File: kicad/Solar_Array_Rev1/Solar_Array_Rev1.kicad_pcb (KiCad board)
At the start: 2 copper layers, 46.9 x 29 mm, 24 parts, among them IC2 NUP4202W1_4INPUT_TVS, IC3 NUP4202W1_4INPUT_TVS, P1 PV_IN, P2 CONN_01X07, Q1 Q_NPN_BCE, U1 LTC2990

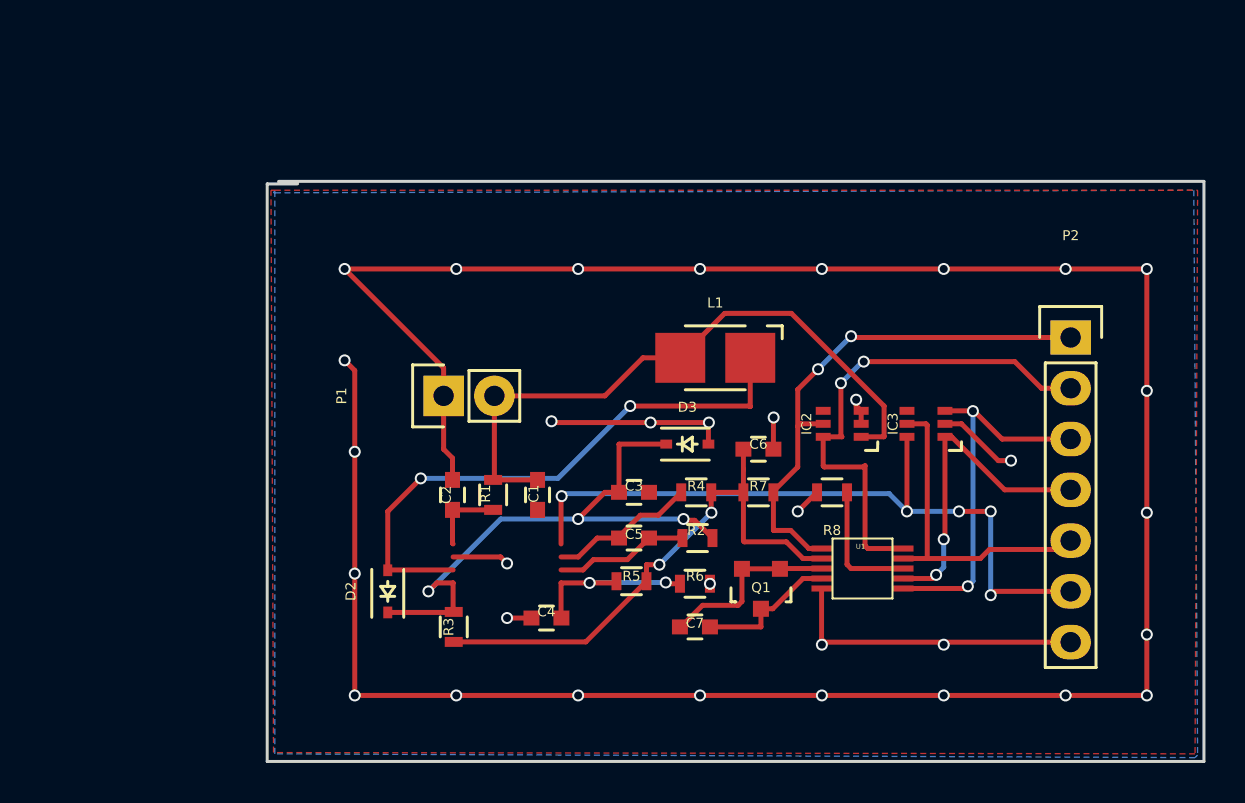
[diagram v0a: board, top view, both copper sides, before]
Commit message: Removed old files, repaired broken schema, finished layout.
-Removed old SVG DRL and  GBR files
-Removed old PDF files
-Fixed broken TVS_4x4 Schematic and updated footprint
-PCB file created
-Board layout finished
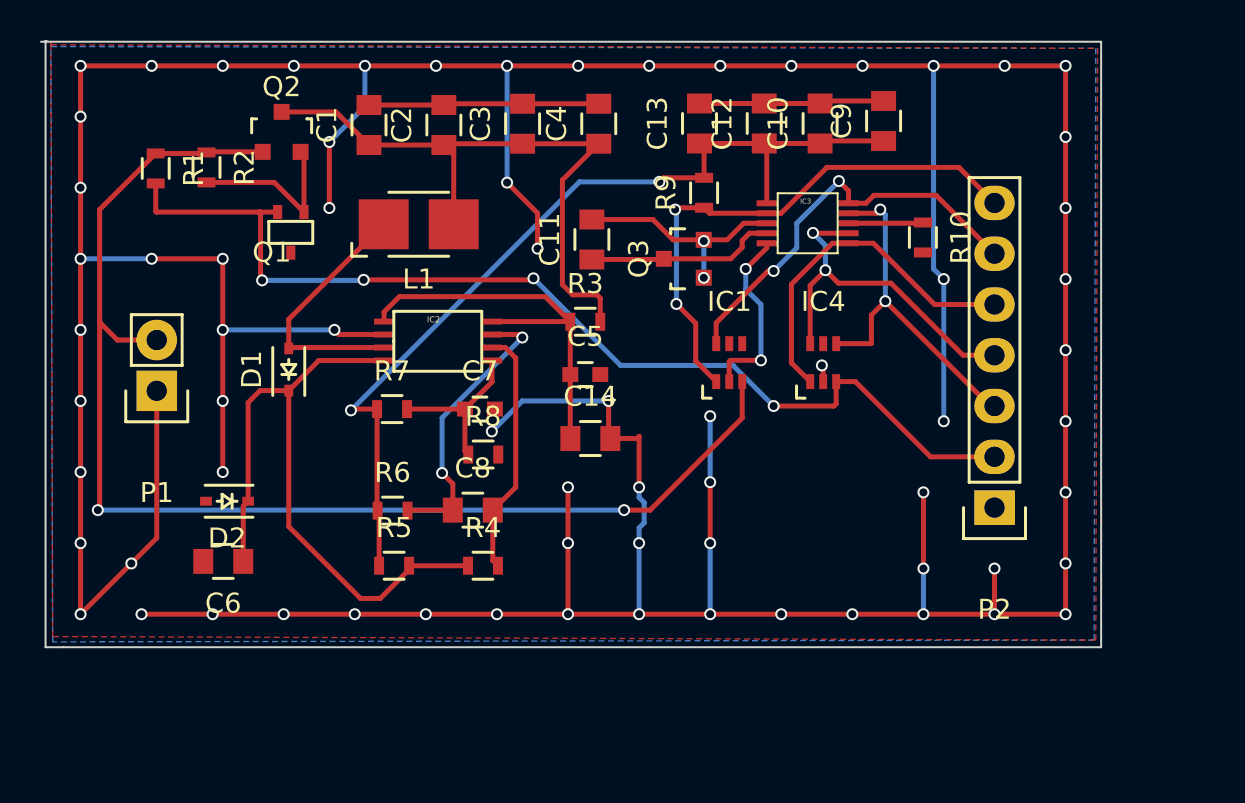
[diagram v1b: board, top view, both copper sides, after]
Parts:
- removed D3: ZENER, Diodes_SMD:SOD-323
- removed U1: LTC2990, Solar:MSOP-10
- added C10: 47u, Capacitors_SMD:C_0805, F.Cu at (151.3, 83.1)
- added C11: 1.2u, Capacitors_SMD:C_0805, F.Cu at (139.9, 89.0)
- added C12: 47u, Capacitors_SMD:C_0805, F.Cu at (148.5, 83.1)
- added C13: 47u, Capacitors_SMD:C_0805, F.Cu at (145.3, 83.1)
- added C14: 1.2u, Capacitors_SMD:C_0805, F.Cu at (139.8, 98.9)
- added C8: 1.2u, Capacitors_SMD:C_0805, F.Cu at (133.9, 102.5)
- added C9: 47u, Capacitors_SMD:C_0805, F.Cu at (154.5, 83.0)
- added D1: D_Schottky, Diodes_SMD:SOD-323, F.Cu at (124.7, 95.5)
- added IC1: TVS_4x4, Solar:SC-70-6, F.Cu at (146.7, 95.1)
- added IC4: TVS_4x4, TO_SOT_Packages_SMD:SC-70-6, F.Cu at (151.4, 95.1)
- added Q2: Q_PMOS_DGS, TO_SOT_Packages_SMD:SOT-23, F.Cu at (124.4, 83.6)
- added Q3: Q_NPN_BCE, TO_SOT_Packages_SMD:SOT-23, F.Cu at (144.5, 89.9)
- added R10: 10k, Resistors_SMD:R_0603, F.Cu at (156.4, 88.8)
- added R9: .3, Resistors_SMD:R_0603, F.Cu at (145.5, 86.6)
- C1, C3: value 216u -> 47u; footprint Capacitors_SMD:C_0603 -> Capacitors_SMD:C_0805
- C2: value 8u -> 47u; footprint Capacitors_SMD:C_0603 -> Capacitors_SMD:C_0805
- C4: value 2u -> 47u; footprint Capacitors_SMD:C_0603 -> Capacitors_SMD:C_0805
- C5: value 1u -> 6.8u
- C6: footprint Capacitors_SMD:C_0603 -> Capacitors_SMD:C_0805
- C7: value 1u -> 2u
- D2: value D_Schottky -> ZENER
- IC2: value NUP4202W1_4INPUT_TVS -> SPV1040; footprint TO_SOT_Packages_SMD:SC-70-6 -> Solar:TSSOP-8
- IC3: value NUP4202W1_4INPUT_TVS -> LTC2990.1; footprint TO_SOT_Packages_SMD:SC-70-6 -> Solar:MSOP-10
- Q1: value Q_NPN_BCE -> Q_NMOS_DGS; footprint TO_SOT_Packages_SMD:SOT-23 -> TO_SOT_Packages_SMD:SC-70
- R1: value 1k -> 10k
- R2: value 1k -> 100k
- R3: value .274 -> 1k
- R5: value 240 -> .274
- R6: value 80 -> 1k
- R7: value .3 -> 240
- R8: value 10k -> 80
- moved R2 30.8 mm to (120.6, 85.3), turned to 270 degrees
- moved Q1 29.5 mm to (124.8, 88.6)
- moved C6 27.4 mm to (121.4, 105.1), turned to 180 degrees
- moved C4 24.9 mm to (140.2, 83.2), turned to 90 degrees
- moved R1 23.5 mm to (118.1, 85.4), turned to 270 degrees
- moved IC2 20.6 mm to (132.2, 94.0), turned to 0 degrees
- moved C1 20.3 mm to (128.7, 83.2), turned to 90 degrees
- moved C3 19.3 mm to (136.4, 83.2), turned to 90 degrees
- moved R7 18.8 mm to (129.9, 97.4), turned to 0 degrees
- moved C2 18.5 mm to (132.5, 83.2)
- moved R8 17.6 mm to (134.4, 99.7), turned to 0 degrees
- moved R3 16.6 mm to (139.5, 93.1), turned to 0 degrees
- moved L1 16.3 mm to (131.2, 88.2), turned to 0 degrees
- moved R6 15.6 mm to (129.9, 102.5)
- moved C7 15.3 mm to (134.3, 97.4), turned to 0 degrees
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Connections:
- C2 pad 1: Net-(C2-Pad1) -> Net-(C1-Pad1)
- C3 pad 1: Net-(C3-Pad1) -> Net-(C1-Pad1)
- C4 pad 1: Net-(C4-Pad1) -> Net-(C1-Pad1)
- C5 pad 1: Net-(C5-Pad1) -> Net-(C14-Pad1)
- C5 pad 2: Net-(C5-Pad2) -> GND
- C7 pad 2: Net-(C7-Pad2) -> GND
- D2 pad 1: Net-(C3-Pad1) -> Net-(C6-Pad1)
- D2 pad 2: Net-(D2-Pad2) -> GND
- IC2 pad 1: Net-(C1-Pad1) -> Net-(C14-Pad1)
- IC2 pad 3: GND -> Net-(D1-Pad2)
- IC2 pad 4: Net-(IC2-Pad4) -> Net-(C6-Pad1)
- IC2 pad 5: Net-(IC2-Pad5) -> Net-(C7-Pad1)
- IC2 pad 6: Net-(IC2-Pad6) -> Net-(C8-Pad2)
- IC3 pad 1: Net-(IC3-Pad1) -> Net-(C10-Pad1)
- IC3 pad 2: GND -> Net-(IC1-Pad1)
- IC3 pad 3: Net-(IC3-Pad3) -> Net-(C11-Pad2)
- IC3 pad 5: Net-(IC3-Pad5) -> GND
- IC3 pad 6: Net-(IC1-Pad8) -> Net-(IC3-Pad6)
- L1 pad 1: Net-(D2-Pad2) -> Net-(D1-Pad2)
- P1 pad 2: Net-(C1-Pad1) -> Net-(IC1-Pad3)
- P2 pad 1: Net-(IC2-Pad5) -> GND
- P2 pad 2: Net-(IC2-Pad6) -> Net-(IC4-Pad3)
- P2 pad 3: Net-(IC3-Pad3) -> Net-(IC3-Pad9)
- P2 pad 4: Net-(IC3-Pad1) -> Net-(IC3-Pad7)
- P2 pad 5: Net-(IC3-Pad5) -> Net-(IC3-Pad6)
- P2 pad 6: Net-(IC1-Pad8) -> Net-(IC1-Pad4)
- P2 pad 7: GND -> Net-(IC1-Pad1)
- Q1 pad 1: Net-(C7-Pad2) -> Net-(Q1-Pad1)
- Q1 pad 2: Net-(C7-Pad2) -> Net-(IC4-Pad3)
- Q1 pad 3: Net-(C7-Pad1) -> GND
- R1 pad 1: Net-(C2-Pad1) -> Net-(IC1-Pad3)
- R1 pad 2: Net-(C1-Pad1) -> Net-(IC4-Pad3)
- R2 pad 1: Net-(C3-Pad1) -> Net-(IC1-Pad3)
- R2 pad 2: Net-(C5-Pad2) -> Net-(Q1-Pad1)
- R3 pad 1: Net-(C6-Pad1) -> Net-(C14-Pad1)
- R3 pad 2: Net-(C3-Pad1) -> Net-(C1-Pad1)
- R4 pad 2: Net-(C5-Pad1) -> Net-(C8-Pad2)
- R5 pad 1: Net-(C6-Pad1) -> Net-(C10-Pad1)
- R5 pad 2: Net-(C4-Pad1) -> Net-(C6-Pad1)
- R6 pad 1: Net-(C4-Pad1) -> Net-(C10-Pad1)
- R6 pad 2: GND -> Net-(C8-Pad1)
- R7 pad 1: Net-(IC2-Pad5) -> Net-(C10-Pad1)
- R7 pad 2: Net-(C6-Pad1) -> Net-(C7-Pad1)
- R8 pad 1: Net-(R8-Pad1) -> Net-(C7-Pad1)
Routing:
- net GND: track 165.0 -> 299.1 mm, vias 33 -> 72
- net Net-(IC1-Pad3): track 0.00 -> 63.7 mm, vias 0 -> 2
- net Net-(IC4-Pad3): track 0.00 -> 53.1 mm, vias 0 -> 4
- net Net-(C10-Pad1): track 0.00 -> 45.9 mm, vias 0 -> 2
- net Net-(IC1-Pad8): track 36.3 -> 0.00 mm, vias 5 -> 0
- net Net-(C3-Pad1): track 29.6 -> 0.00 mm, vias 3 -> 0
- net Net-(D2-Pad2): track 29.0 -> 0.00 mm, vias 2 -> 0
- net Net-(IC1-Pad1): track 0.00 -> 27.3 mm, vias 0 -> 2
- net Net-(IC2-Pad5): track 26.4 -> 0.00 mm, vias 2 -> 0
- net Net-(IC2-Pad6): track 25.7 -> 0.00 mm, vias 2 -> 0
- net Net-(IC1-Pad4): track 0.00 -> 20.8 mm, vias 0 -> 2
- net Net-(C14-Pad1): track 0.00 -> 20.4 mm
- net Net-(IC3-Pad3): track 19.1 -> 0.00 mm, vias 2 -> 0
- net Net-(IC3-Pad9): track 0.00 -> 18.1 mm, vias 0 -> 2
- net Net-(IC3-Pad7): track 0.00 -> 18.1 mm, vias 0 -> 2
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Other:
- board size 46.9 x 29 mm -> 53 x 30.3 mm
- rule pad_to_mask_clearance: 0.001 -> 0

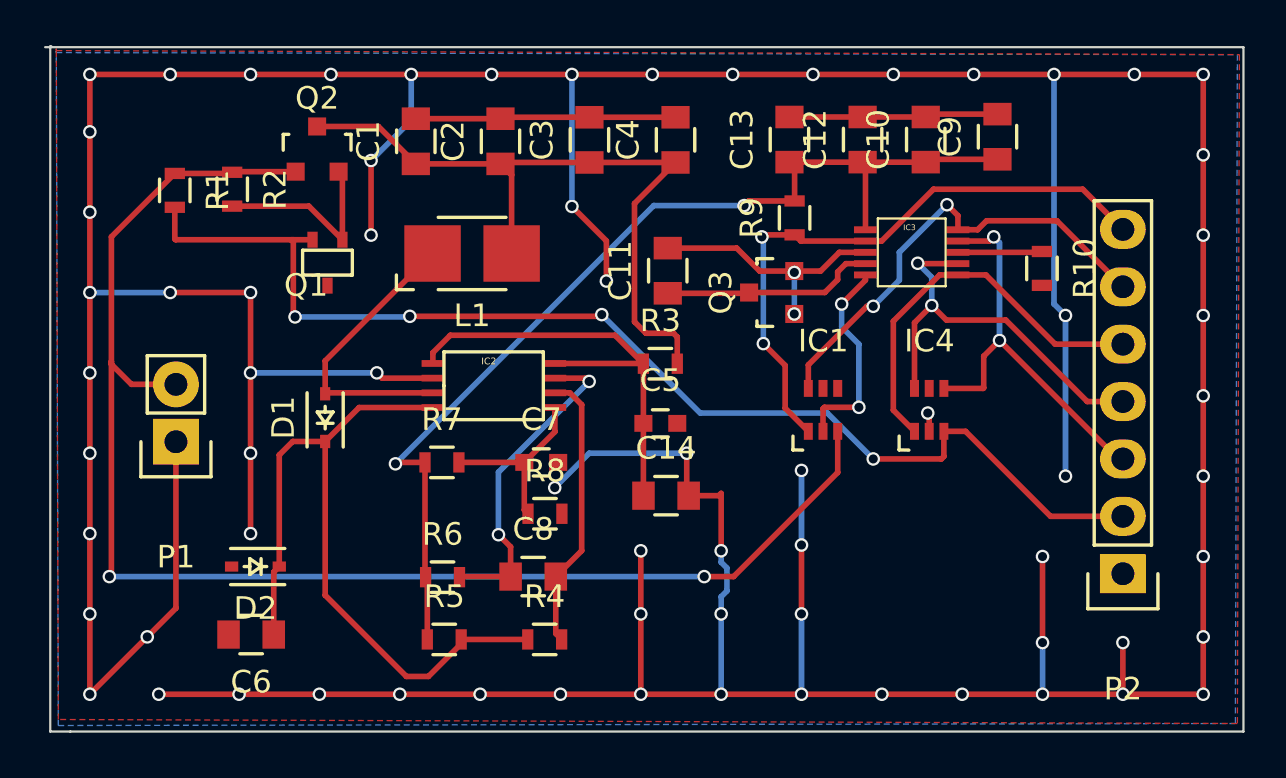
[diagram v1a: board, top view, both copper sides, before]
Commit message: Removed D2.  Set R9 as NP resistor and tied sensor to R5.
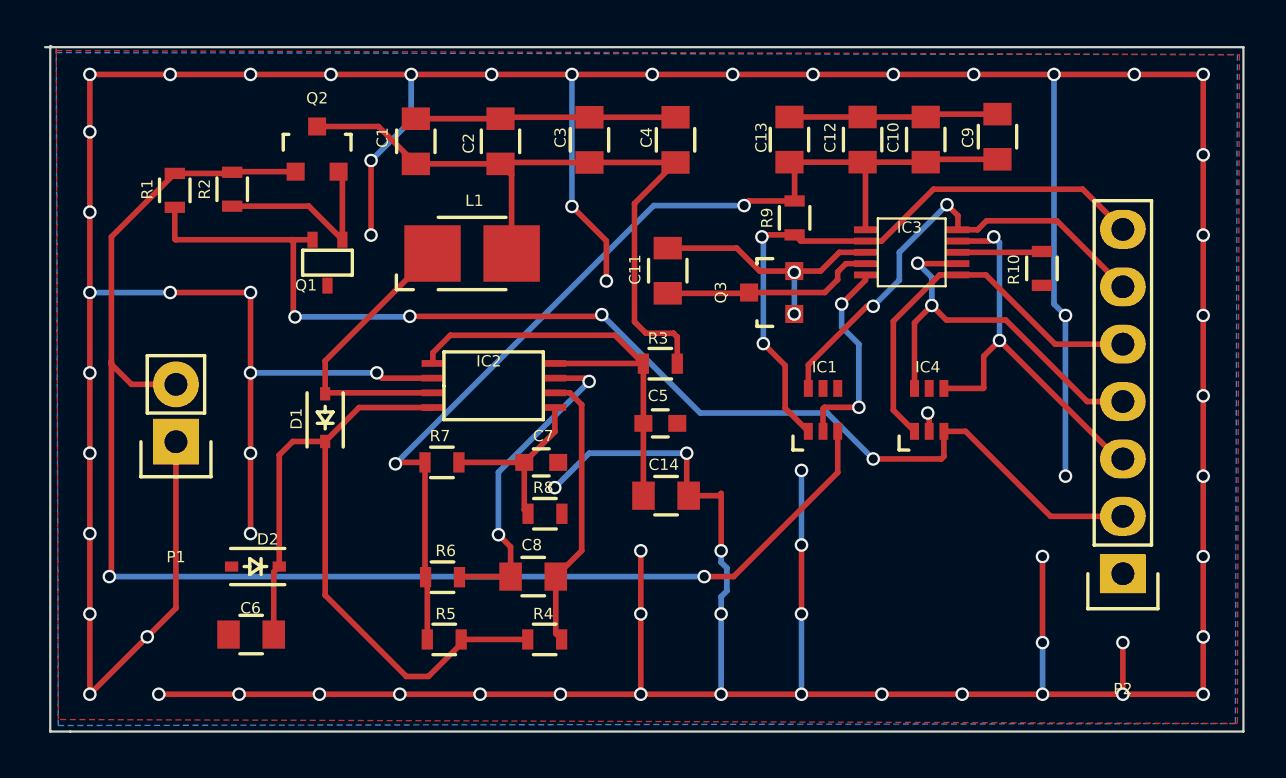
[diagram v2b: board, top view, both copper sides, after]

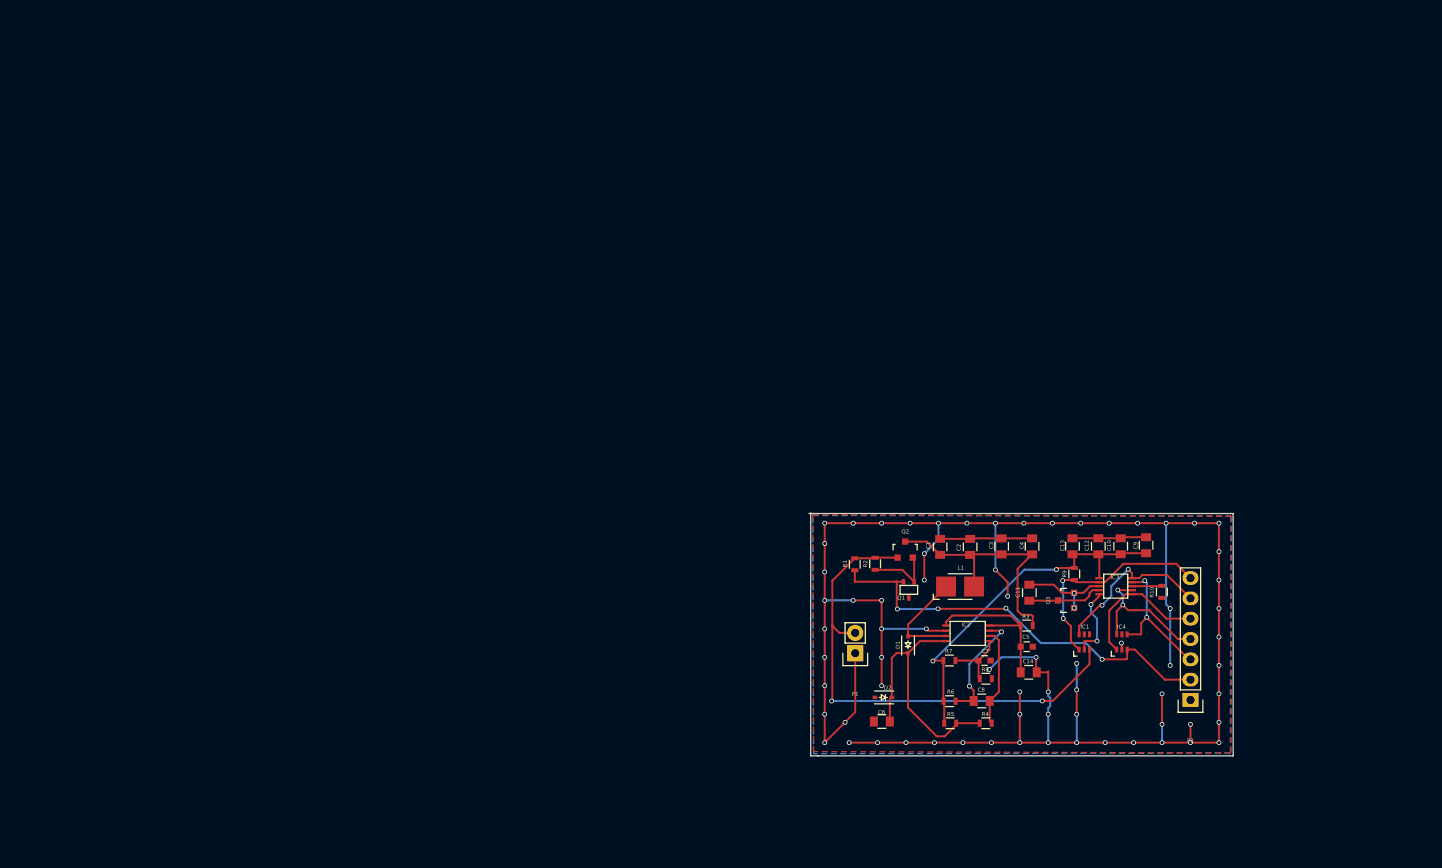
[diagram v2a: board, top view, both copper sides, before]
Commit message: Optimized for power. -Changed Vctrl divider on SPV1040 to limit power dissipation and current. -Removed needlessly large input capacitor. -Lowered cap value to recommended values near temp sensing transistor -Added 2ohm sense resistor for LTC2990 cutting power dissipation by 83.3% -Cleared old board and regenerated netlists. -Fixed LTC2990 to represent new schematic us under "LTC2990.2"
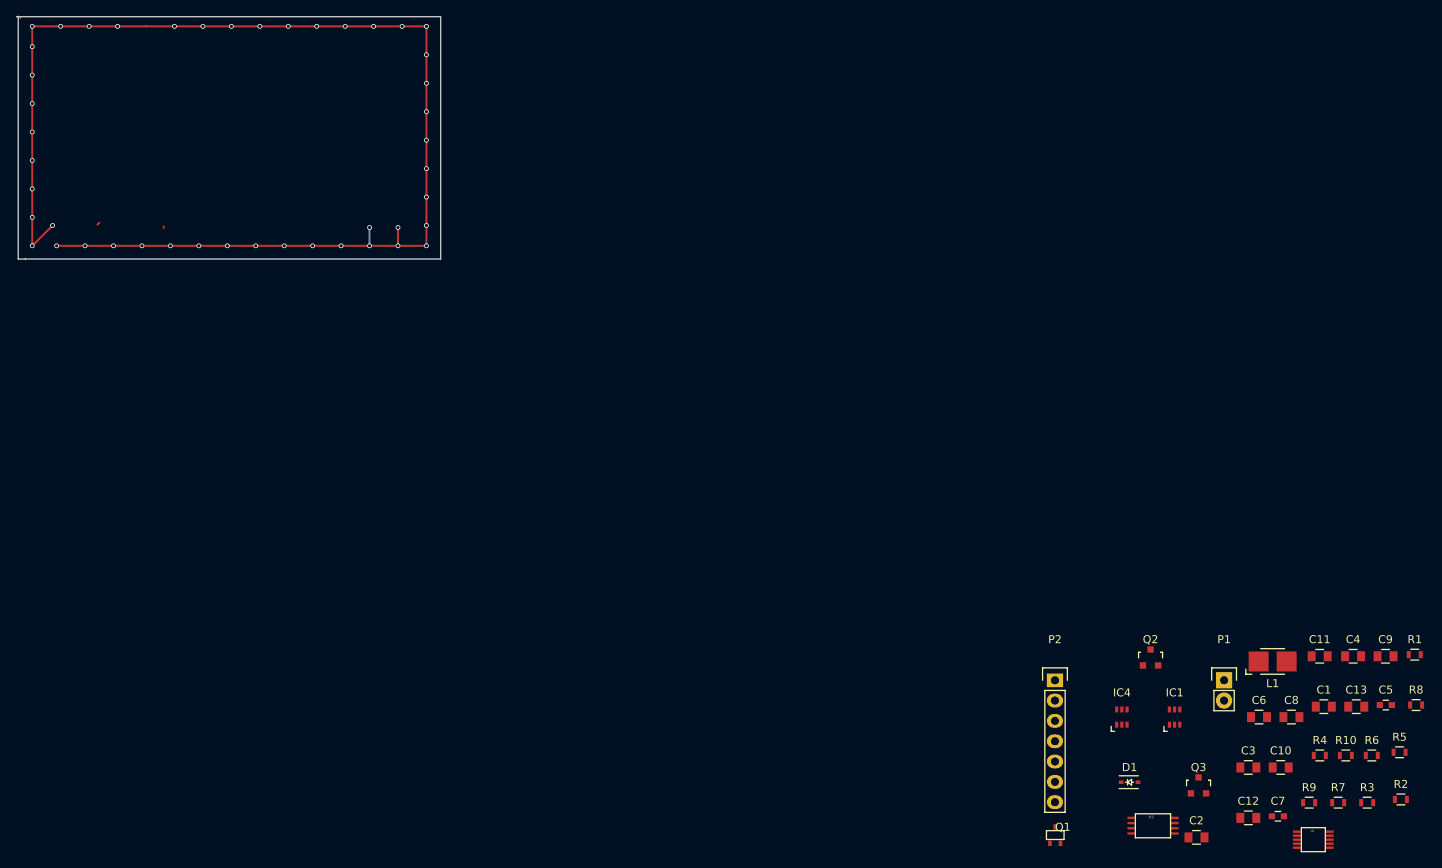
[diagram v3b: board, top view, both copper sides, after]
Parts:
- removed C14: 1.2u, Capacitors_SMD:C_0805
- removed D2: ZENER, Diodes_SMD:SOD-323
- removed IC3: LTC2990.1, Solar:MSOP-10
- added U1: LTC2990, Solar:MSOP-10, F.Cu at (175.4, 119.8)
- C11: value 1.2u -> 470p
- C5: value 6.8u -> .1u
- C6: value 22u -> 10u
- C7: value 2u -> .1u
- IC1: footprint Solar:SC-70-6 -> TO_SOT_Packages_SMD:SC-70-6
- Q1: value Q_NMOS_DGS -> 2N7002WT1GOSCT
- Q2: value Q_PMOS_DGS -> NTR1P02T1GOSCT
- Q3: value Q_NPN_BCE -> MMBT3904
- R7: value 240 -> 820k
- R8: value 80 -> 270k
- R9: value .3 -> 2
- moved R2 72.0 mm to (186.3, 114.8), turned to 0 degrees
- moved R1 70.9 mm to (188.1, 96.7), turned to 0 degrees
- moved R5 56.3 mm to (186.2, 108.9)
- moved R8 53.9 mm to (188.2, 103.0)
- moved R6 53.2 mm to (182.7, 109.3)
- moved C1 52.0 mm to (176.7, 103.2), turned to 0 degrees
- moved R7 51.7 mm to (178.5, 115.2)
- moved R3 48.0 mm to (182.1, 115.2)
- moved C6 47.2 mm to (168.6, 104.5), turned to 0 degrees
- moved P1 46.2 mm to (164.2, 99.9), turned to 0 degrees
- moved C2 46.0 mm to (160.8, 119.5), turned to 0 degrees
- moved C5 45.5 mm to (184.4, 103.0)
- moved C4 42.4 mm to (180.3, 96.9), turned to 0 degrees
- moved R4 42.0 mm to (176.2, 109.3)
- moved C7 41.5 mm to (170.9, 116.9)
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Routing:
- net GND: track 299.1 -> 0.00 mm, vias 72 -> 0
- net (no net): track 0.00 -> 159.1 mm, vias 0 -> 46
- net Net-(IC1-Pad3): track 63.7 -> 0.00 mm, vias 2 -> 0
- net Net-(IC4-Pad3): track 53.1 -> 0.00 mm, vias 4 -> 0
- net Net-(C10-Pad1): track 45.9 -> 0.00 mm, vias 2 -> 0
- net Net-(C6-Pad1): track 33.8 -> 0.00 mm
- net Net-(C1-Pad1): track 32.1 -> 0.00 mm
- net Net-(IC1-Pad1): track 27.3 -> 0.00 mm, vias 2 -> 0
- net Net-(IC1-Pad4): track 20.8 -> 0.00 mm, vias 2 -> 0
- net Net-(C5-Pad1): track 20.4 -> 0.00 mm
- net Net-(IC4-Pad4): track 18.1 -> 0.00 mm, vias 2 -> 0
- net Net-(IC4-Pad6): track 18.1 -> 0.00 mm, vias 2 -> 0
- net Net-(IC4-Pad1): track 17.5 -> 0.00 mm
- net Net-(C8-Pad1): track 14.4 -> 0.00 mm, vias 2 -> 0
- net Net-(D1-Pad2): track 13.0 -> 0.00 mm
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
